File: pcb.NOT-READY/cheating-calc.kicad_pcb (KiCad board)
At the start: 2 copper layers, 72 x 22 mm, 16 parts, among them J1 Conn_01x04, J2 Conn_01x04, Q1 MMBF170, Q2 MMBF170, U1 ESP32-C3-MINI-1-N4, U2 AP7215-33YG-13

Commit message: update cap
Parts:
- C1, C2: value CL21B105KBFNNNE -> CL21B105KPFNNNE

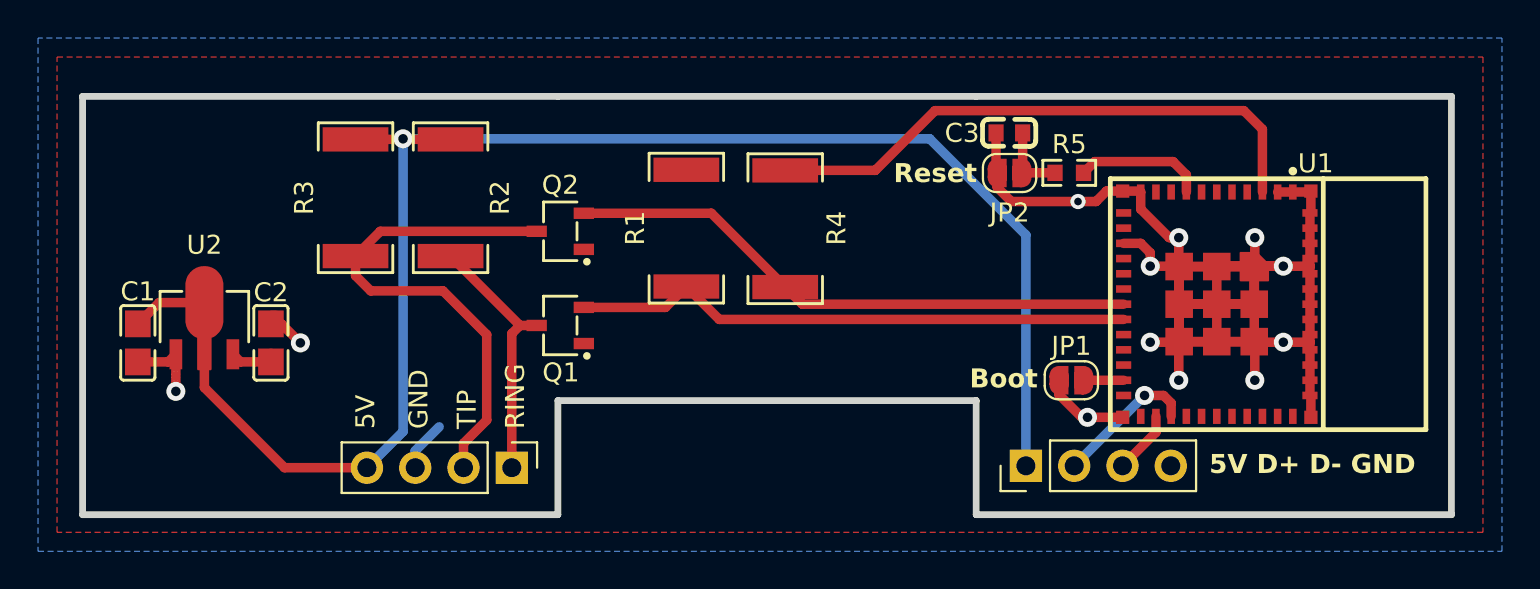
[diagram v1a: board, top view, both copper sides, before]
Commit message: Update PCB to add programming pins
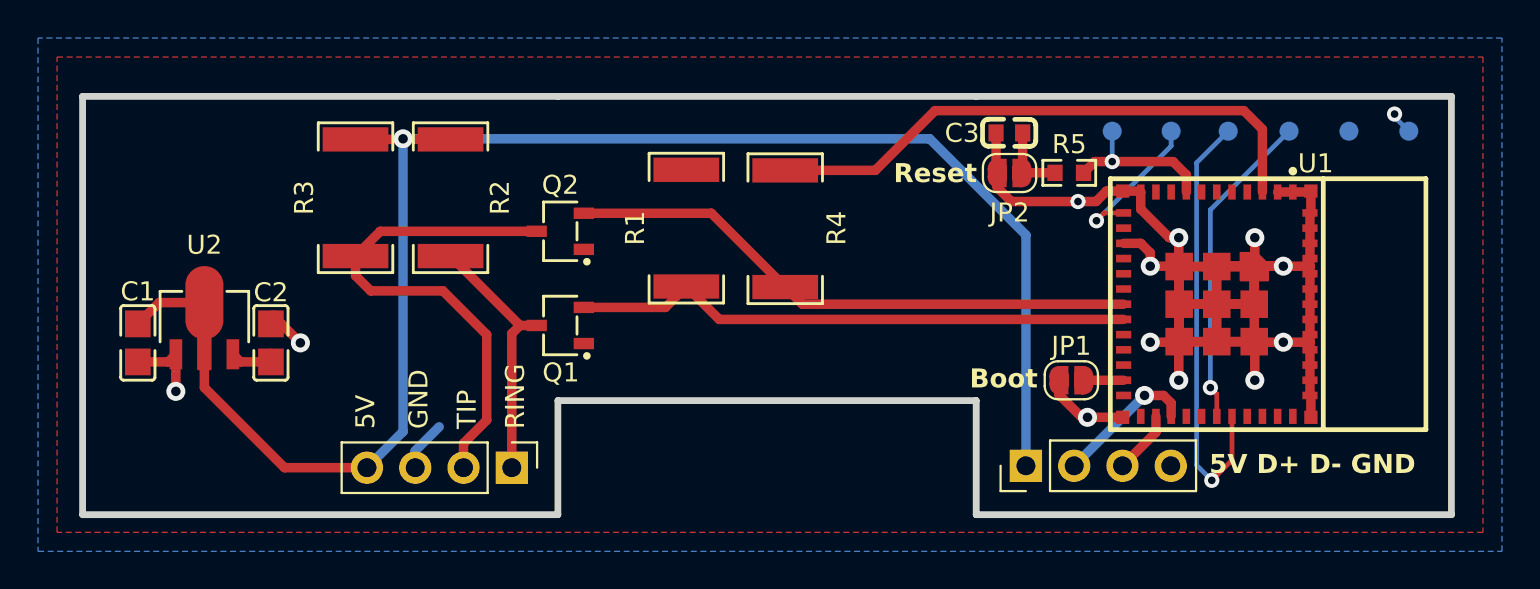
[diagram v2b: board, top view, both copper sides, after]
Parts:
- added TP1: TestPoint, TestPoint:TestPoint_Pad_D1.0mm, B.Cu at (155.1, 53.9)
- added TP2: TestPoint, TestPoint:TestPoint_Pad_D1.0mm, B.Cu at (151.9, 53.9)
- added TP3: TestPoint, TestPoint:TestPoint_Pad_D1.0mm, B.Cu at (148.8, 53.9)
- added TP4: TestPoint, TestPoint:TestPoint_Pad_D1.0mm, B.Cu at (145.6, 53.9)
- added TP5: TestPoint, TestPoint:TestPoint_Pad_D1.0mm, B.Cu at (142.6, 53.9)
- added TP6: TestPoint, TestPoint:TestPoint_Pad_D1.0mm, B.Cu at (139.5, 53.9)
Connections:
- U1 pad 12: unconnected-(U1-IO0-Pad12) -> Net-(U1-IO0)
- U1 pad 30: unconnected-(U1-RXD0-Pad30) -> Net-(U1-RXD0)
- U1 pad 31: unconnected-(U1-TXD0-Pad31) -> Net-(U1-TXD0)
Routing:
- net Net-(U1-TXD0): track 0.00 -> 23.2 mm, vias 0 -> 1
- net Net-(U1-RXD0): track 0.00 -> 16.9 mm, vias 0 -> 1
- net Net-(U1-IO0): track 0.00 -> 7.93 mm, vias 0 -> 1
- net Net-(U1-EN): track 6.84 -> 8.44 mm, vias 0 -> 1
- net +3.3V: track 32.3 -> 33.6 mm, vias 0 -> 1

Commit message: update
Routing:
- net GND: track 105.5 -> 106.5 mm

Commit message: update
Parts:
- moved TP1 0.50 mm to (154.6, 53.9)
- moved TP2 0.35 mm to (151.6, 53.9)
- moved TP3 0.20 mm to (148.6, 53.9)
- moved TP6 0.10 mm to (139.6, 53.9)
